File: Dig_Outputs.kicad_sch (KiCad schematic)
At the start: 30 parts, among them Q1 BSS806, Q1 MMBT3904, Q2 MMBT3904, Q3 MMBT3904, Q4 MMBT3904

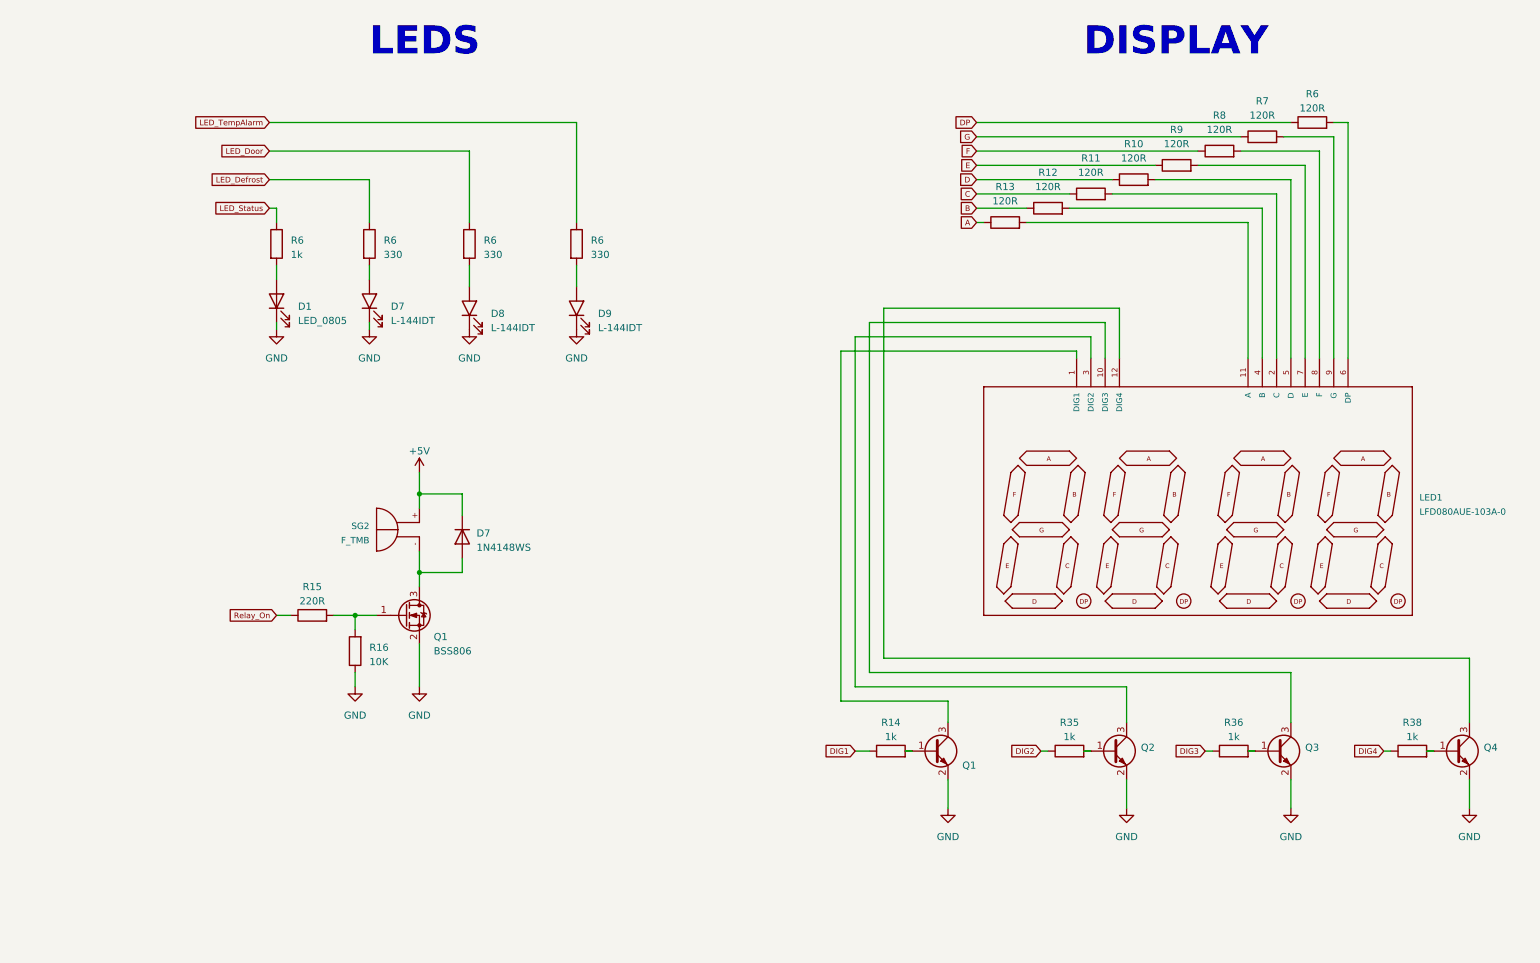
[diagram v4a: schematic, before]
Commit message: SCH:Se modifica los leds y nombres, en este punto, posibilemente se cambie el tamaño de la placa
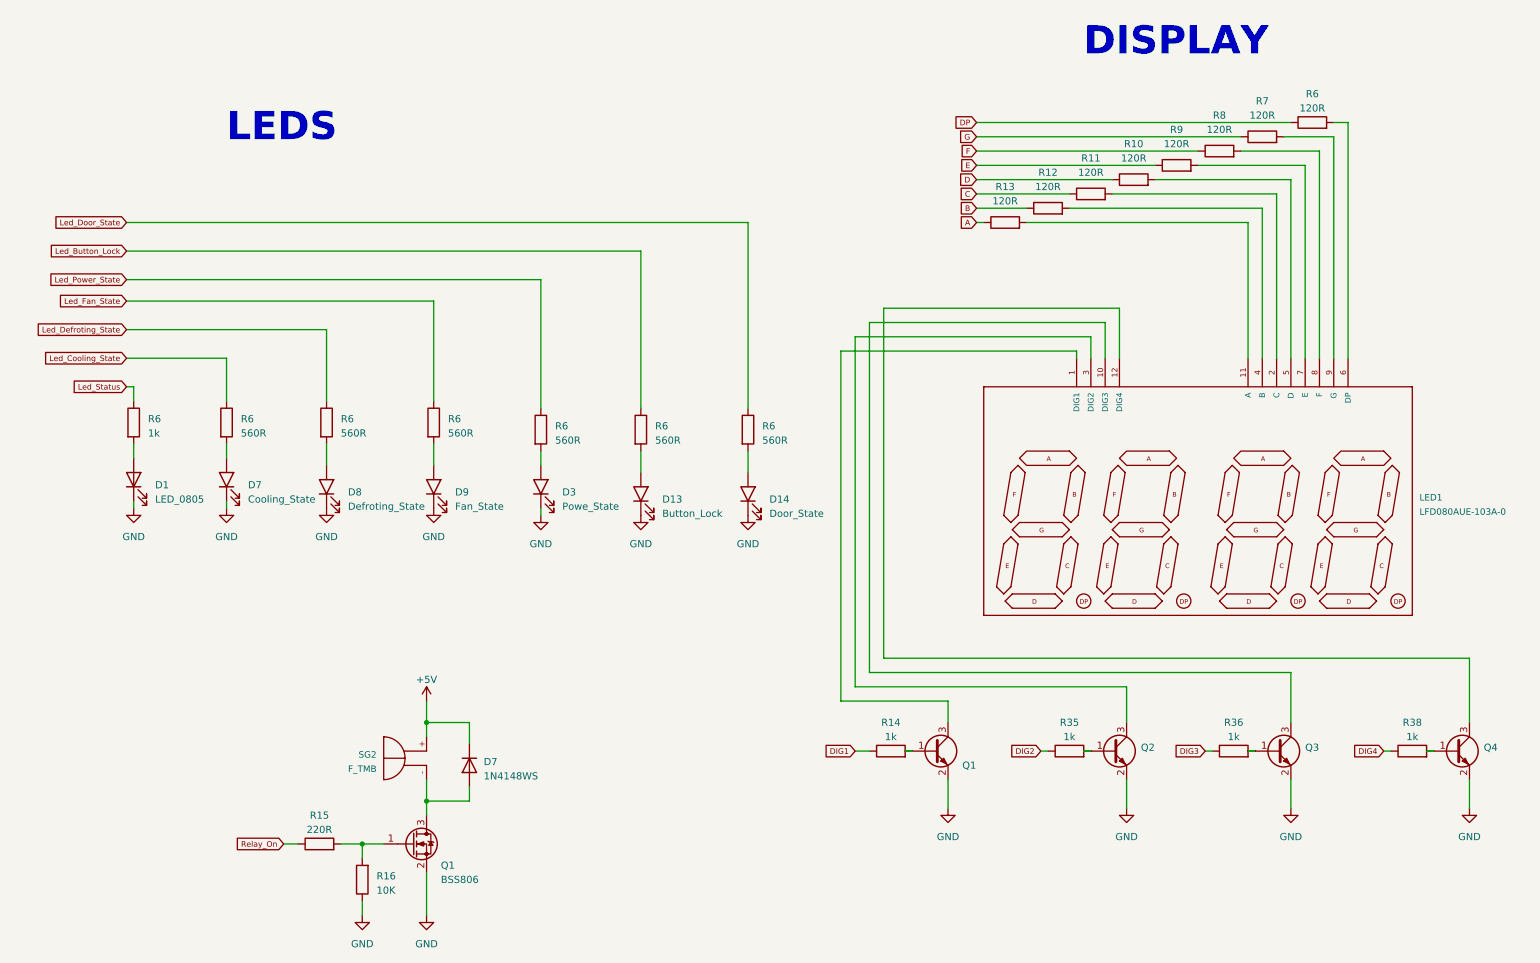
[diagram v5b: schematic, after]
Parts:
- added D13: Button_Lock, 1-Led:LED_3mm, symbol 1-Led:LED_Rect
- added D14: Door_State, 1-Led:LED_3mm, symbol 1-Led:LED_Rect
- added D3: Powe_State, 1-Led:LED_3mm, symbol 1-Led:LED_Rect
- added R6 (x3): 560R, 1-Resistor:R_0805_2012Metric, symbol 1-Resistor:R_0603
- D7: value L-144IDT -> Cooling_State; footprint 1-Led:LED_3.9x1.9mm -> 1-Led:LED_3mm
- D8: value L-144IDT -> Defroting_State; footprint 1-Led:LED_3.9x1.9mm -> 1-Led:LED_3mm
- D9: value L-144IDT -> Fan_State; footprint 1-Led:LED_3.9x1.9mm -> 1-Led:LED_3mm
- R6: value 330 -> 560R
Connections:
- net GND: now also D13.K, D14.K, D3.K
- net LED_Defrost renamed Led_Cooling_State
- net LED_Door renamed Led_Defroting_State
- net LED_Status renamed Led_Status
- net LED_TempAlarm renamed Led_Fan_State
- new net: D13.A, R6.2
- new net: D14.A, R6.2
- new net: D3.A, R6.2
- new net Led_Button_Lock: R6.1
- new net Led_Door_State: R6.1
- new net Led_Power_State: R6.1
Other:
- moved on the sheet: D1, D7, D8, D9, Q1, R15, R16, R6, SG2
